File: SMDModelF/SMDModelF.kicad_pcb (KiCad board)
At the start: 2 copper layers, 158.4 x 41.7 mm, 45 parts, among them J1 Model F Ribbon Cable, J2 PadsToShort, J3 EXPANSION HEADER, J4 3178 Ribbon Cable, J6 MODEL F AT LOCKLIGHTS HEADER, U1 MCP4921-E, U2 LM339A, U3 74AHC595, U4 74AHC595, U5 ProMicro, U6 LM339A

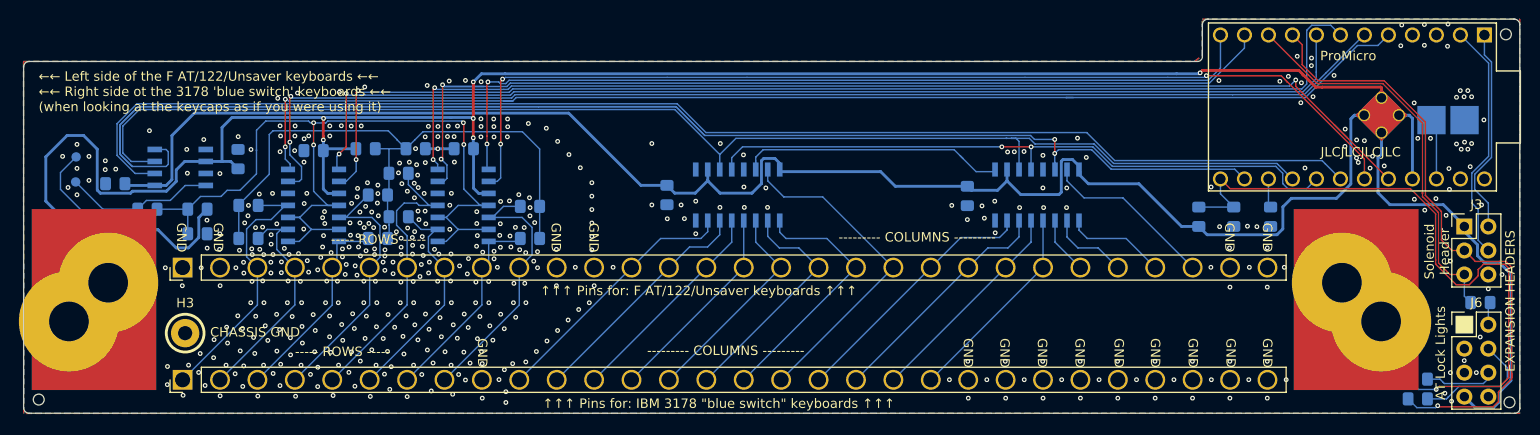
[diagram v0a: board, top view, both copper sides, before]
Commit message: Added extra columns
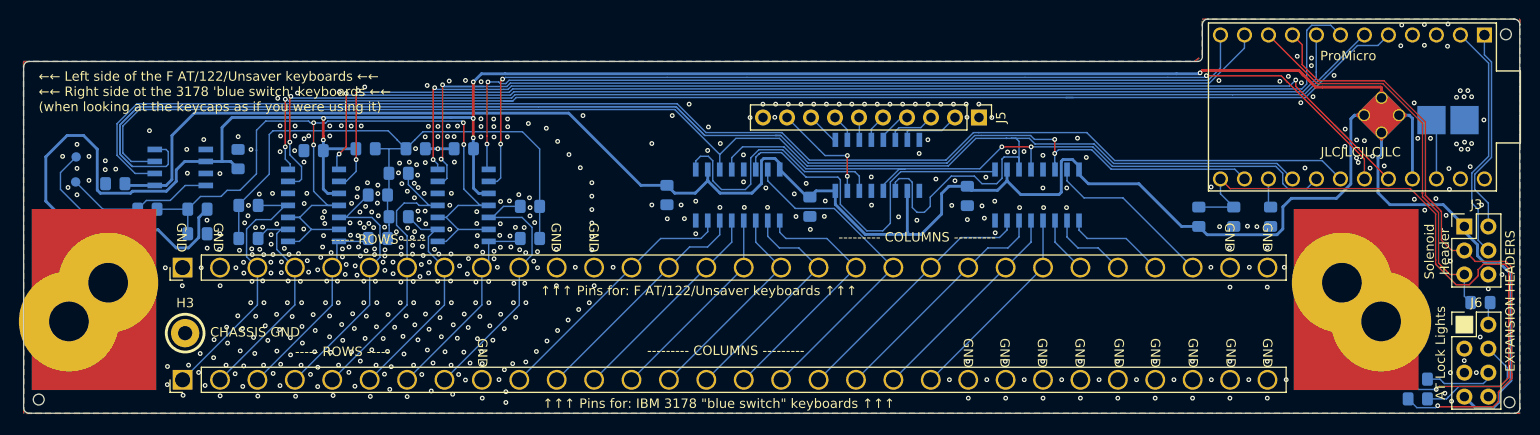
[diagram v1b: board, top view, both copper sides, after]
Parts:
- added C5: 0U1, Capacitor_SMD:C_0805_2012Metric_Pad1.15x1.40mm_HandSolder, B.Cu at (160.1, 72.6)
- added J5: Conn_01x10, Connector_PinHeader_2.54mm:PinHeader_1x10_P2.54mm_Vertical, F.Cu at (178.0, 63.2)
- added U7: 74AHC595, Package_SO:SOIC-16_3.9x9.9mm_P1.27mm, B.Cu at (167.3, 68.3)
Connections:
- U4 pad 9: Net-(U4-Pad9) -> SERIALOUT2
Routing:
- net SERIALOUT2: track 0.00 -> 27.2 mm
- net CLOCK: track 141.9 -> 167.6 mm
- net +5VD: track 168.1 -> 180.0 mm
- net COL17: track 0.00 -> 11.8 mm, vias 0 -> 2
- net SERIALOUT1: track 29.2 -> 37.9 mm
- net COL24: track 0.00 -> 6.56 mm
- net LOADCOL: track 69.4 -> 74.9 mm
- net COL23: track 0.00 -> 5.29 mm
- net COL22: track 0.00 -> 4.03 mm
- net COL18: track 0.00 -> 3.74 mm
- net MOSI: track 207.5 -> 210.5 mm
- net COL19: track 0.00 -> 2.91 mm
- net COL21: track 0.00 -> 2.88 mm
- net COL20: track 0.00 -> 2.45 mm
- net ~SELECTDAC: track 142.0 -> 144.5 mm
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
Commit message: Ported over some changes from the 'standard' model F controller, to make 3d rendering look better
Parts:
- J3: footprint Connector_PinHeader_2.54mm:PinHeader_2x03_P2.54mm_Vertical -> TH-XWhatsIt:PinHeader_2x03_P2.54mm_Vertical_3dhorizontal
